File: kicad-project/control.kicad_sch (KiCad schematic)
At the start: 30 parts, among them SW1 RST_SW, U1 RP2040

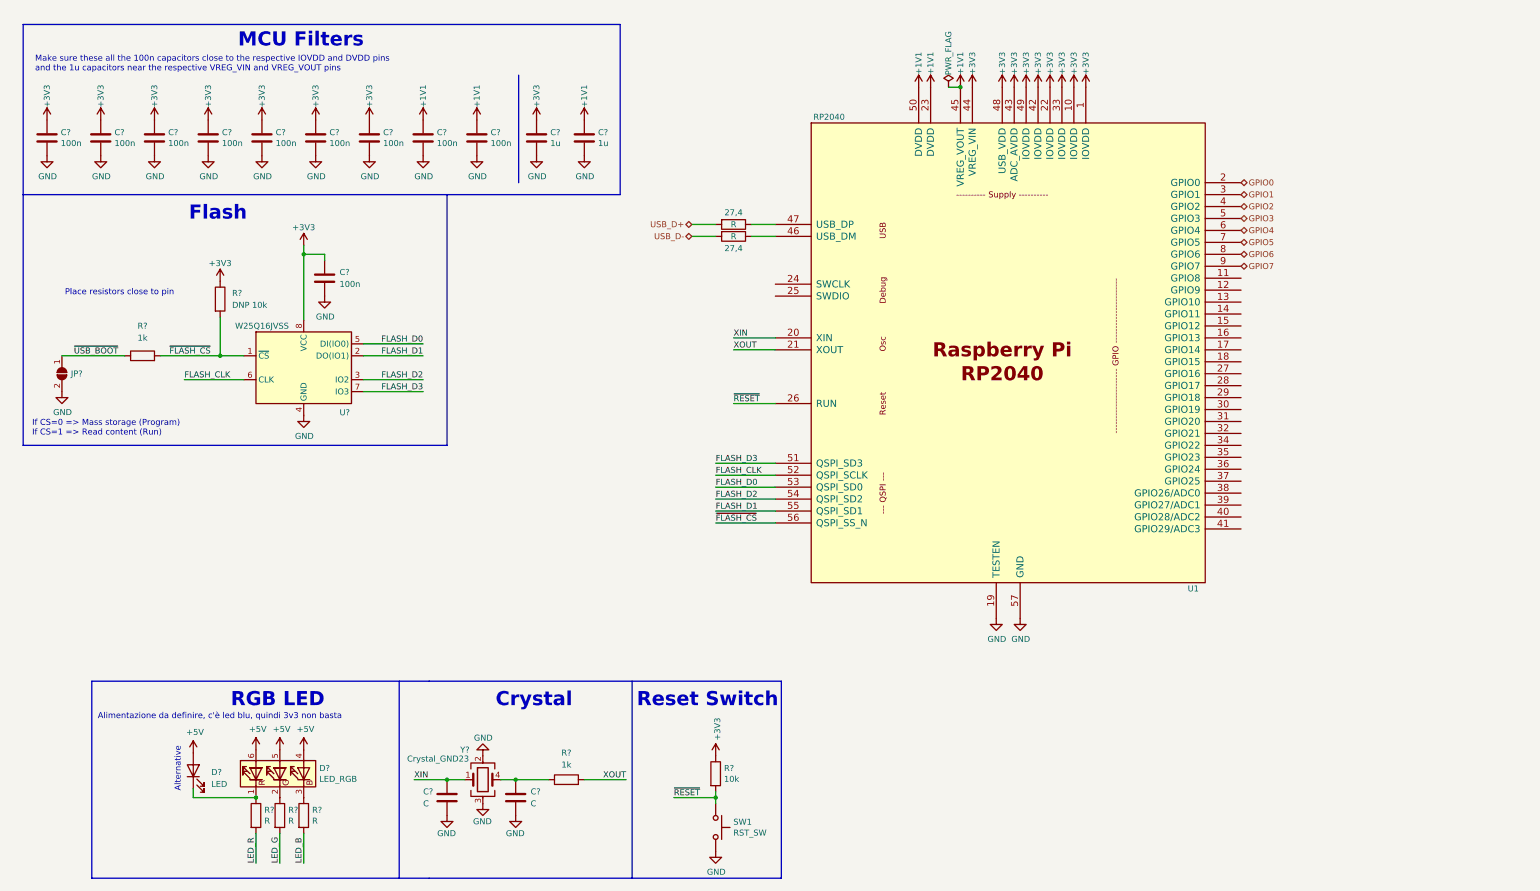
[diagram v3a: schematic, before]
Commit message: hw: add limit switches, dual power input, actuation sheet, debug and expansion connectors and connect sheets
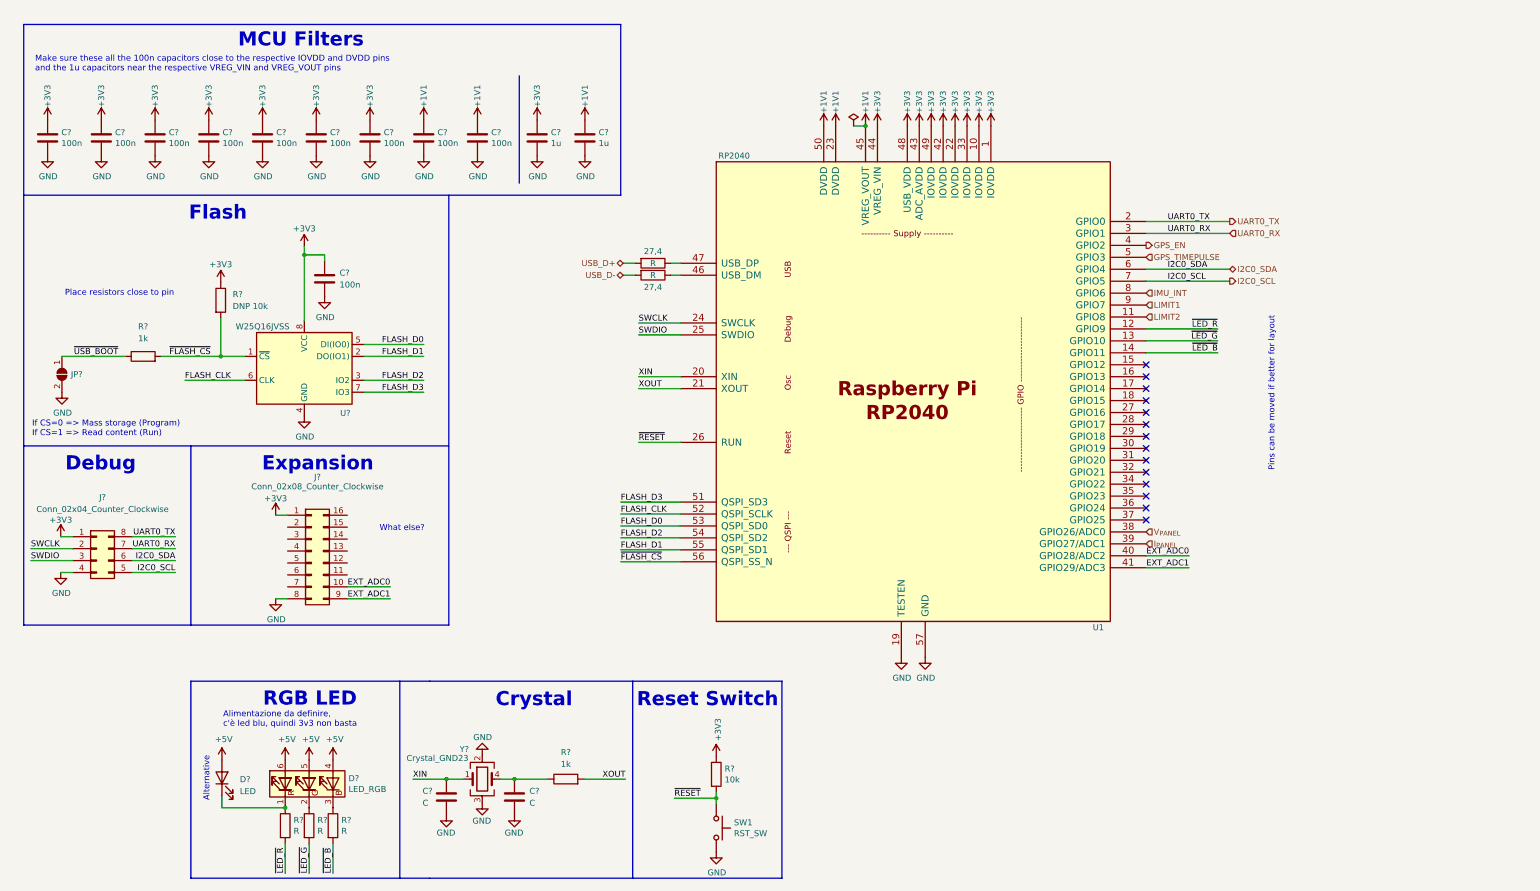
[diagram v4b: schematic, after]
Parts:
- added J?: Conn_02x04_Counter_Clockwise, symbol Connector_Generic:Conn_02x04_Counter_Clockwise
- added J?: Conn_02x08_Counter_Clockwise, symbol Connector_Generic:Conn_02x08_Counter_Clockwise
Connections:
- net LED_B is gone; now on net ~{LED_B}: R?.2
- net LED_G is gone; now on net ~{LED_G}: R?.2
- net LED_R is gone; now on net ~{LED_R}: R?.2
- net +3V3: now also J?.1 (Pin_1), J?.1 (Pin_1)
- net GND: now also J?.4 (Pin_4), J?.8 (Pin_8)
- net LIMIT2: now reaches U1.11 (GPIO8)
- net ~{LED_R}: now reaches U1.12 (GPIO9)
- net ~{LED_G}: now reaches U1.13 (GPIO10)
- net ~{LED_B}: now reaches U1.14 (GPIO11)
- net SWCLK: now reaches U1.24 (SWCLK)
- net SWCLK: now also J?.2 (Pin_2)
- net SWDIO: now reaches U1.25 (SWDIO)
- net SWDIO: now also J?.3 (Pin_3)
- net V_{PANEL}: now reaches U1.38 (GPIO26/ADC0)
- net I_{PANEL}: now reaches U1.39 (GPIO27/ADC1)
- net EXT_ADC0: now reaches U1.40 (GPIO28/ADC2)
- net EXT_ADC0: now also J?.10 (Pin_10)
- net EXT_ADC1: now reaches U1.41 (GPIO29/ADC3)
- net EXT_ADC1: now also J?.9 (Pin_9)
- net GPIO0 renamed UART0_TX
- net UART0_TX: now also J?.8 (Pin_8)
- net GPIO1 renamed UART0_RX
- net UART0_RX: now also J?.7 (Pin_7)
- net GPIO2 renamed GPS_EN
- net GPIO3 renamed GPS_TIMEPULSE
- net GPIO4 renamed I2C0_SDA
- net I2C0_SDA: now also J?.6 (Pin_6)
- net GPIO5 renamed I2C0_SCL
- net I2C0_SCL: now also J?.5 (Pin_5)
- net GPIO6 renamed IMU_INT
- net GPIO7 renamed LIMIT1
- no-connect marks 0 -> 14
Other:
- note added: "Debug"
- note added: "Expansion"
- note added: "Pins can be moved if better for layout"
- note added: "What else?"
- moved on the sheet: 27,4, D?, R?, U1

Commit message: hw: schematic updates
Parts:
- added BZ?: (no value), symbol Device:Buzzer
- added Q?: PDTC114Y, symbol Transistor_BJT:DTC114Y
- added R?: (no value), symbol Device:R
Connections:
- net +5V: now also BZ?.1 (-), R?.1
- net GND: now also Q?.2 (E)
- net BUZZ_EN: now reaches U1.28 (GPIO17)
- net BUZZ_EN: now also Q?.1 (B)
- net I2C1_SDA: now reaches U1.29 (GPIO18)
- net I2C1_SDA: now also J?.12 (Pin_12)
- net I2C1_SCL: now reaches U1.30 (GPIO19)
- net I2C1_SCL: now also J?.11 (Pin_11)
- new net: BZ?.2 (+), Q?.3 (C), R?.2
- no-connect marks 14 -> 11
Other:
- note added: "BUZZER"
- note added: "Contare se GPIO bastano"
- note added: "I2C1: IMU I2C0: ???"
- note added: "What else? Perchè cosi grande? IMU va qua considerando che va messo sul pannello."
- note removed: "What else?"
- moved on the sheet: C?, D?, JP?, R?, SW1, U1, U?, Y?

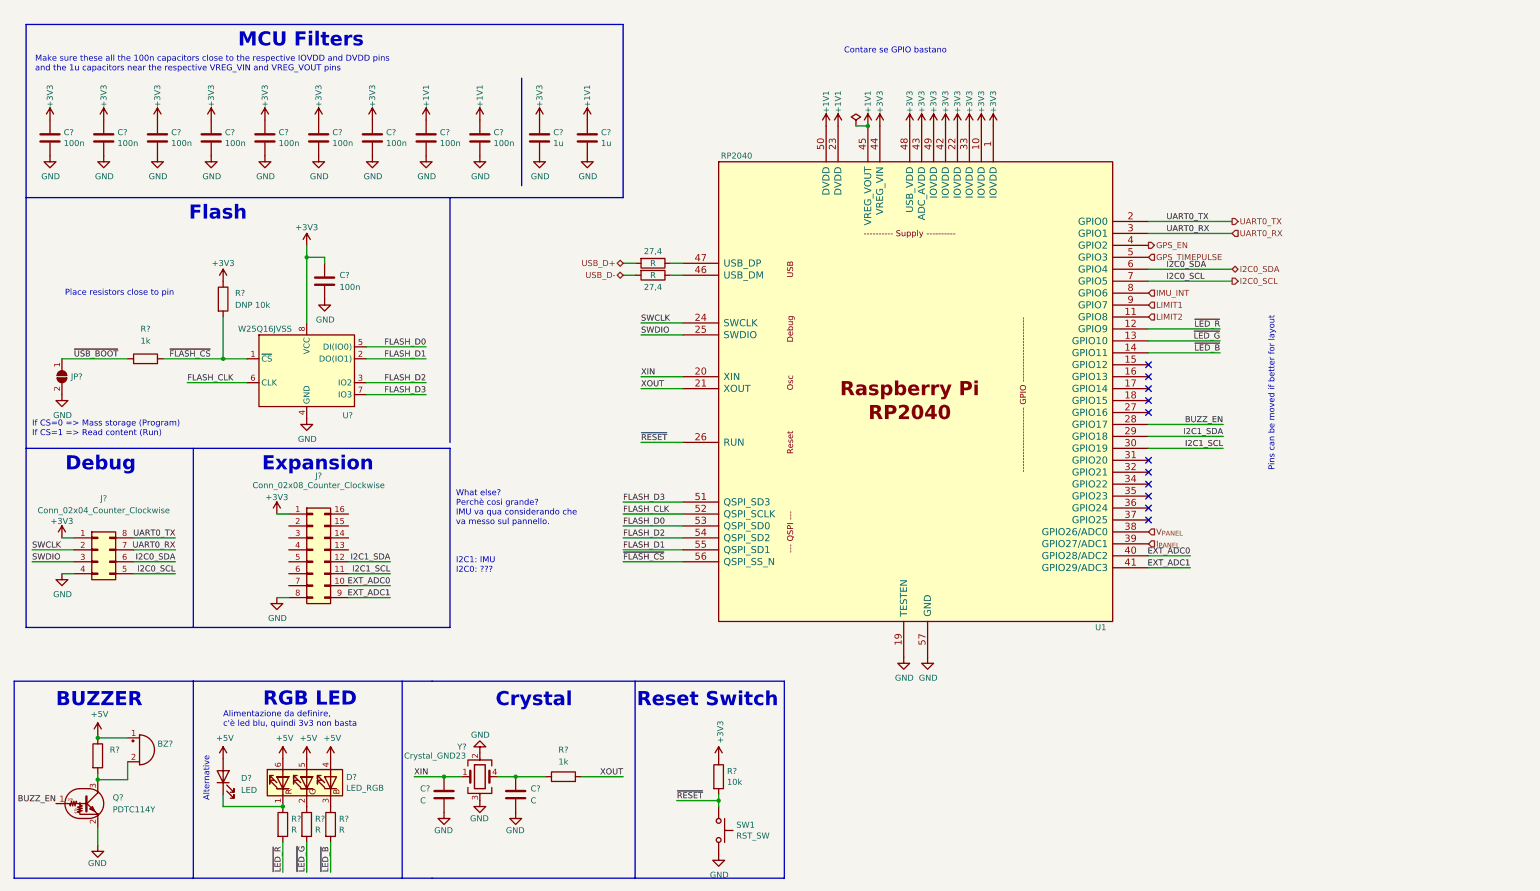
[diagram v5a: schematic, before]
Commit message: hw: connect filtering capacitor near vdd pin
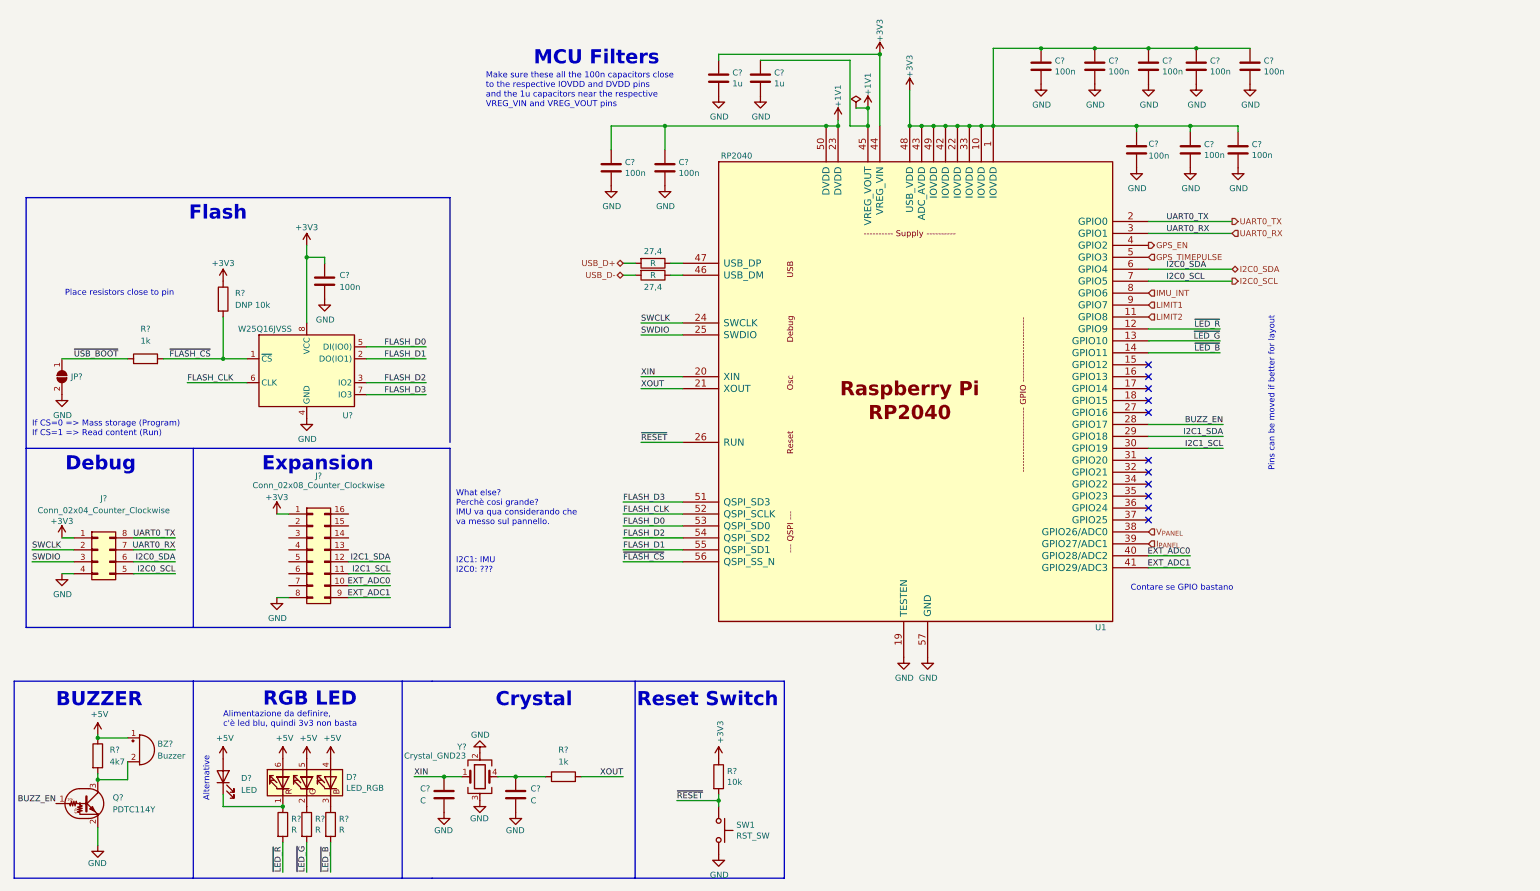
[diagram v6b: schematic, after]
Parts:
- removed C? (x7): 100n, Capacitor_SMD:C_0603_1608Metric, symbol Device:C
- added C? (x8): 100n, Capacitor_SMD:C_0603_1608Metric, symbol Device:C
- BZ?: value (none) -> Buzzer
- R?: value (none) -> 4k7
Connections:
- net +3V3: now also C?.1, C?.1, C?.1, C?.1, C?.1, C?.1, C?.1, C?.1
- net GND: now also C?.2, C?.2, C?.2, C?.2, C?.2, C?.2, C?.2, C?.2
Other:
- moved on the sheet: C?

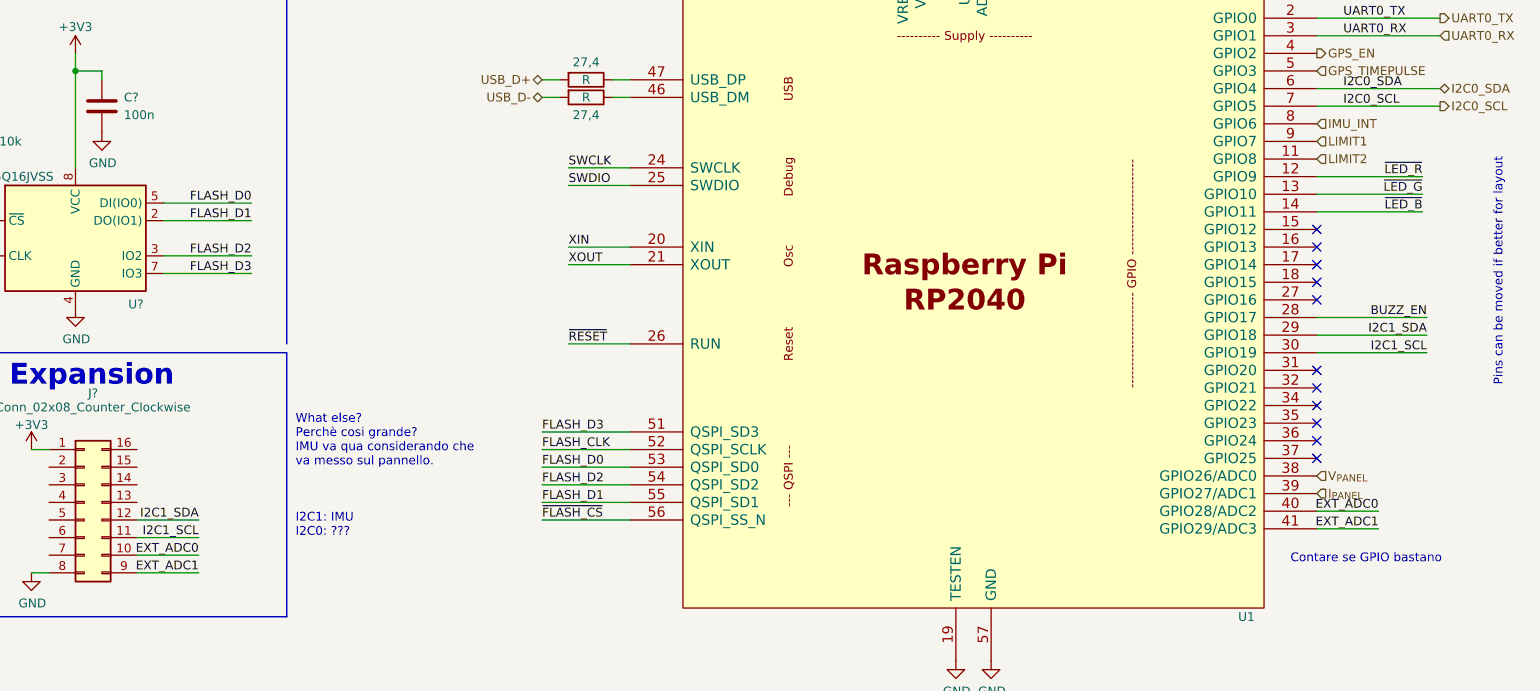
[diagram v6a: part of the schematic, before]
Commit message: hw: update schematic pt. 2
add switching enable resistor, change usb inductor to ferrite bead, add OR gate and microstepping solder jumpers to motor driver, remove i2c and backup supply solder jumper from GPS, add ferrite bead to GPS, remove limit switches and other small changes
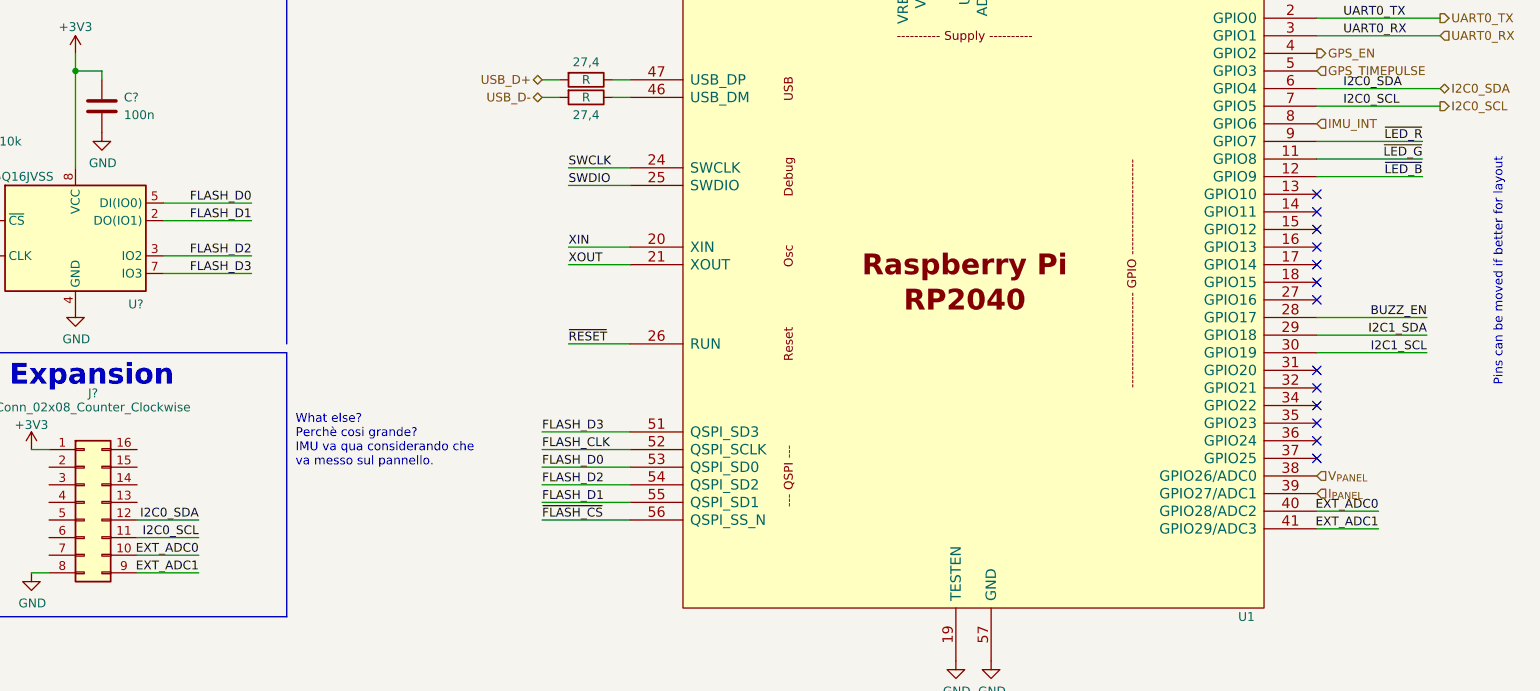
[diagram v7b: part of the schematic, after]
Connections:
- net LIMIT1 is gone; now on net ~{LED_R}: U1.9 (GPIO7)
- net LIMIT2 is gone; now on net ~{LED_G}: U1.11 (GPIO8)
- net I2C0_SCL: now also J?.11 (Pin_11)
- net I2C0_SDA: now also J?.12 (Pin_12)
- net I2C1_SCL: no longer J?.11 (Pin_11)
- net I2C1_SDA: no longer J?.12 (Pin_12)
- net ~{LED_B}: now also U1.12 (GPIO9); no longer U1.14 (GPIO11)
- net ~{LED_G}: no longer U1.13 (GPIO10)
- net ~{LED_R}: no longer U1.12 (GPIO9)
- no-connect marks 11 -> 13
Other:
- note removed: "Contare se GPIO bastano"
- note removed: "I2C1: IMU I2C0: ???"
